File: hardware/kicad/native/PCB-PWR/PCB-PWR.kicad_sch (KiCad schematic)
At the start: 60 parts, among them J1 PWR_INPUT_43045-0213, J2 MAIN_PWR_43045-1202_12PIN, Q1 CSD18540Q5B, U1 LM74700QDBVRQ1, U2 INA226AIDGSR, U3 LMR604403SRAKR 3V8, U4 LMR604403SRAKR 3V3 AON, U5 TPS7A2018PDBVR 1V8_MIC

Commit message: pcb(pwr): bind shared Molex 12-pin footprint
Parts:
- J2: footprint (none) -> DioneyaMain:Molex_43045-1202_MicroFit-12_RA
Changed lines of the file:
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@@
       (effects (font (size 1 1)))
     )
-    (property "Footprint" "" (id 2) (at 198.12 120.22 0)
+    (property "Footprint" "DioneyaMain:Molex_43045-1202_MicroFit-12_RA" (id 2) (at 198.12 120.22 0)
       (effects (font (size 1 1)) hide)
     )

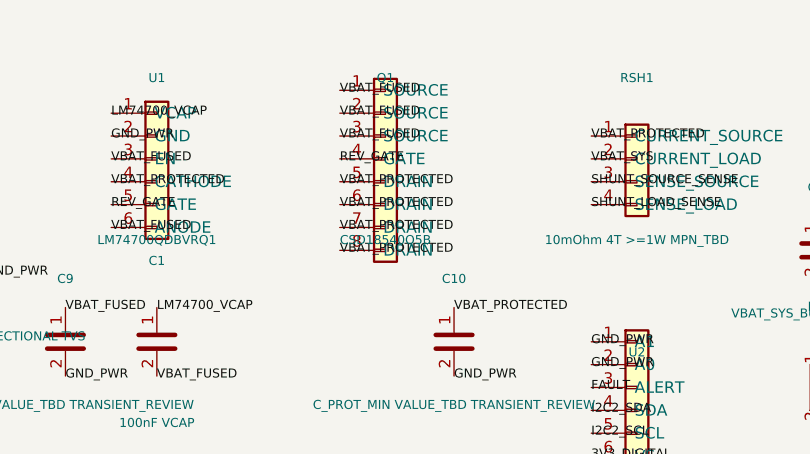
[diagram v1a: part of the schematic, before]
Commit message: fix(pwr): correct CSD18540 physical pin map
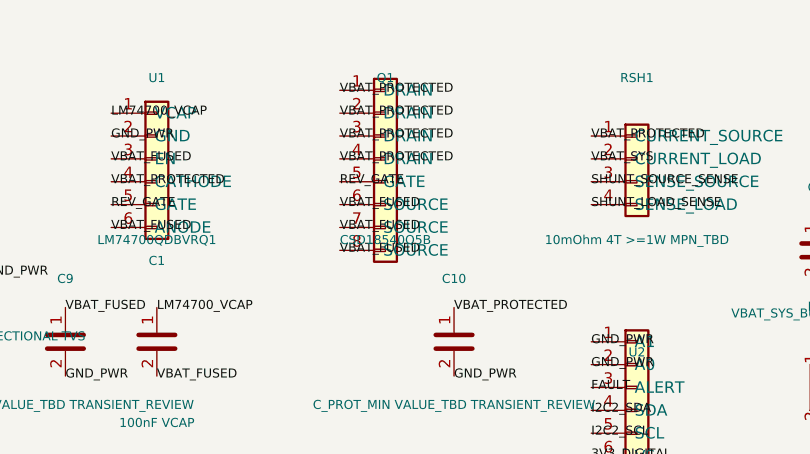
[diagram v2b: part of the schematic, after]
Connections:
- net REV_GATE: now also Q1.5 (GATE); no longer Q1.4 (GATE)
- net VBAT_FUSED: now also Q1.6 (SOURCE), Q1.7 (SOURCE), Q1.8 (SOURCE); no longer Q1.1 (SOURCE), Q1.2 (SOURCE), Q1.3 (SOURCE)
- net VBAT_PROTECTED: now also Q1.1 (DRAIN), Q1.2 (DRAIN), Q1.3 (DRAIN), Q1.4 (DRAIN); no longer Q1.5 (DRAIN), Q1.6 (DRAIN), Q1.7 (DRAIN), Q1.8 (DRAIN)
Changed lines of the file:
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@@
     (effects (font (size 1 1)))
   )
-  (label "VBAT_FUSED" (at 104.14 30.48 0)
+  (label "VBAT_PROTECTED" (at 104.14 30.48 0)
     (effects (font (size 1 1)))
   )
-  (label "VBAT_FUSED" (at 104.14 33.02 0)
+  (label "VBAT_PROTECTED" (at 104.14 33.02 0)
     (effects (font (size 1 1)))
   )
-  (label "VBAT_FUSED" (at 104.14 35.56 0)
+  (label "VBAT_PROTECTED" (at 104.14 35.56 0)
     (effects (font (size 1 1)))
   )
-  (label "REV_GATE" (at 104.14 38.1 0)
+  (label "VBAT_PROTECTED" (at 104.14 38.1 0)
     (effects (font (size 1 1)))
   )
-  (label "VBAT_PROTECTED" (at 104.14 40.64 0)
+  (label "REV_GATE" (at 104.14 40.64 0)
     (effects (font (size 1 1)))
   )
-  (label "VBAT_PROTECTED" (at 104.14 43.18 0)
+  (label "VBAT_FUSED" (at 104.14 43.18 0)
     (effects (font (size 1 1)))
   )
-  (label "VBAT_PROTECTED" (at 104.14 45.72 0)
+  (label "VBAT_FUSED" (at 104.14 45.72 0)
     (effects (font (size 1 1)))
   )
-  (label "VBAT_PROTECTED" (at 104.14 48.26 0)
+  (label "VBAT_FUSED" (at 104.14 48.26 0)
     (effects (font (size 1 1)))
   )

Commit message: Revert "fix(pwr): correct CSD18540 physical pin map"
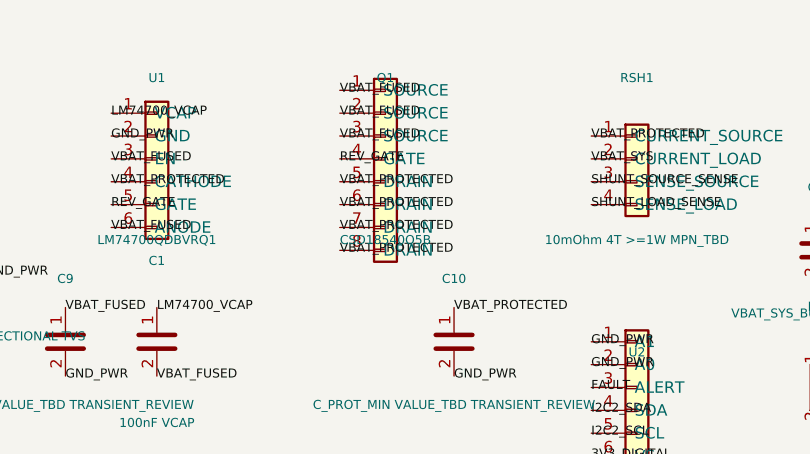
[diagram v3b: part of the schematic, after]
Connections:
- net REV_GATE: now also Q1.4 (GATE); no longer Q1.5 (GATE)
- net VBAT_FUSED: now also Q1.1 (SOURCE), Q1.2 (SOURCE), Q1.3 (SOURCE); no longer Q1.6 (SOURCE), Q1.7 (SOURCE), Q1.8 (SOURCE)
- net VBAT_PROTECTED: now also Q1.5 (DRAIN), Q1.6 (DRAIN), Q1.7 (DRAIN), Q1.8 (DRAIN); no longer Q1.1 (DRAIN), Q1.2 (DRAIN), Q1.3 (DRAIN), Q1.4 (DRAIN)
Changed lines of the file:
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@@
     (effects (font (size 1 1)))
   )
-  (label "VBAT_PROTECTED" (at 104.14 30.48 0)
+  (label "VBAT_FUSED" (at 104.14 30.48 0)
     (effects (font (size 1 1)))
   )
-  (label "VBAT_PROTECTED" (at 104.14 33.02 0)
+  (label "VBAT_FUSED" (at 104.14 33.02 0)
     (effects (font (size 1 1)))
   )
-  (label "VBAT_PROTECTED" (at 104.14 35.56 0)
+  (label "VBAT_FUSED" (at 104.14 35.56 0)
     (effects (font (size 1 1)))
   )
-  (label "VBAT_PROTECTED" (at 104.14 38.1 0)
+  (label "REV_GATE" (at 104.14 38.1 0)
     (effects (font (size 1 1)))
   )
-  (label "REV_GATE" (at 104.14 40.64 0)
+  (label "VBAT_PROTECTED" (at 104.14 40.64 0)
     (effects (font (size 1 1)))
   )
-  (label "VBAT_FUSED" (at 104.14 43.18 0)
+  (label "VBAT_PROTECTED" (at 104.14 43.18 0)
     (effects (font (size 1 1)))
   )
-  (label "VBAT_FUSED" (at 104.14 45.72 0)
+  (label "VBAT_PROTECTED" (at 104.14 45.72 0)
     (effects (font (size 1 1)))
   )
-  (label "VBAT_FUSED" (at 104.14 48.26 0)
+  (label "VBAT_PROTECTED" (at 104.14 48.26 0)
     (effects (font (size 1 1)))
   )

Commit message: pcb(pwr): control CSD18540 footprint
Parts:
- Q1: footprint (none) -> DioneyaPWR:CSD18540Q5B_DNK
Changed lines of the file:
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@@
       (effects (font (size 1 1)))
     )
-    (property "Footprint" "" (id 2) (at 109.22 49.1 0)
+    (property "Footprint" "DioneyaPWR:CSD18540Q5B_DNK" (id 2) (at 109.22 49.1 0)
       (effects (font (size 1 1)) hide)
     )

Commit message: pcb(pwr): control LMR60440 land pattern
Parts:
- U3, U4: footprint (none) -> DioneyaPWR:LMR60440_RAK0009A
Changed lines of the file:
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@@
       (effects (font (size 1 1)))
     )
-    (property "Footprint" "" (id 2) (at 55.88 112.6 0)
+    (property "Footprint" "DioneyaPWR:LMR60440_RAK0009A" (id 2) (at 55.88 112.6 0)
       (effects (font (size 1 1)) hide)
     )
@@
       (effects (font (size 1 1)))
     )
-    (property "Footprint" "" (id 2) (at 121.92 112.6 0)
-      (effects (font (size 1 1)) hide)
-    )
+    (property "Footprint" "DioneyaPWR:LMR60440_RAK0009A" (id 2) (at 121.92 112.6 0)
+      (effects (font (size 1 1)) hide)
+    )

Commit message: pcb(pwr): control TI support IC land patterns
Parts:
- U1: footprint Package_TO_SOT_SMD:SOT-23-6 -> DioneyaPWR:TI_DBV0006A_SOT23-6
- U2: footprint Package_SO:VSSOP-10_3x3mm_P0.5mm -> DioneyaPWR:TI_DGS0010A_VSSOP10
- U5: footprint Package_TO_SOT_SMD:SOT-23-5 -> DioneyaMain:TI_DBV0005A_SOT23-5
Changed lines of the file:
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@@
       (effects (font (size 1 1)))
     )
-    (property "Footprint" "Package_TO_SOT_SMD:SOT-23-6" (id 2) (at 83.82 49.1 0)
+    (property "Footprint" "DioneyaPWR:TI_DBV0006A_SOT23-6" (id 2) (at 83.82 49.1 0)
       (effects (font (size 1 1)) hide)
     )
@@
       (effects (font (size 1 1)))
     )
-    (property "Footprint" "Package_SO:VSSOP-10_3x3mm_P0.5mm" (id 2) (at 137.16 79.58 0)
+    (property "Footprint" "DioneyaPWR:TI_DGS0010A_VSSOP10" (id 2) (at 137.16 79.58 0)
       (effects (font (size 1 1)) hide)
     )
@@
       (effects (font (size 1 1)))
     )
-    (property "Footprint" "Package_TO_SOT_SMD:SOT-23-5" (id 2) (at 68.58 168.48 0)
-      (effects (font (size 1 1)) hide)
-    )
+    (property "Footprint" "DioneyaMain:TI_DBV0005A_SOT23-5" (id 2) (at 68.58 168.48 0)
+      (effects (font (size 1 1)) hide)
+    )

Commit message: pcb(pwr): control remaining component land patterns
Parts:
- J1: footprint (none) -> DioneyaPWR:Molex_43045-0213_MicroFit-2_Vertical
- L1, L2: value 4.7uH >=6A MPN_TBD -> XAL7030-472MEC 4.7uH; footprint (none) -> DioneyaPWR:Coilcraft_XAL7030_472
- RSH1: value 10mOhm 4T >=1W MPN_TBD -> WSK2512R0100FEA 10mOhm 1% 1W 4T; footprint (none) -> DioneyaPWR:Vishay_WSK2512_4T_T1.19mm
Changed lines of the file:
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@@
       (effects (font (size 1 1)))
     )
-    (property "Footprint" "" (id 2) (at 25.4 49.1 0)
-      (effects (font (size 1 1)) hide)
-    )
-    (property "Datasheet" "Molex Micro-Fit 3.0" (id 3) (at 25.4 51.1 0)
+    (property "Footprint" "DioneyaPWR:Molex_43045-0213_MicroFit-2_Vertical" (id 2) (at 25.4 49.1 0)
+      (effects (font (size 1 1)) hide)
+    )
+    (property "Datasheet" "Molex SD-43045-005 Rev.G1" (id 3) (at 25.4 51.1 0)
       (effects (font (size 1 1)) hide)
     )
@@
       (effects (font (size 1 1)))
     )
-    (property "Value" "10mOhm 4T >=1W MPN_TBD" (id 1) (at 137.16 47.1 0)
-      (effects (font (size 1 1)))
-    )
-    (property "Footprint" "" (id 2) (at 137.16 49.1 0)
-      (effects (font (size 1 1)) hide)
-    )
-    (property "Datasheet" "Review-A Kelvin authority" (id 3) (at 137.16 51.1 0)
+    (property "Value" "WSK2512R0100FEA 10mOhm 1% 1W 4T" (id 1) (at 137.16 47.1 0)
+      (effects (font (size 1 1)))
+    )
+    (property "Footprint" "DioneyaPWR:Vishay_WSK2512_4T_T1.19mm" (id 2) (at 137.16 49.1 0)
+      (effects (font (size 1 1)) hide)
+    )
+    (property "Datasheet" "Vishay WSK2512 document 30108" (id 3) (at 137.16 51.1 0)
       (effects (font (size 1 1)) hide)
     )
@@
       (effects (font (size 1 1)))
     )
-    (property "Value" "4.7uH >=6A MPN_TBD" (id 1) (at 81.28 105.52 0)
-      (effects (font (size 1 1)))
-    )
-    (property "Footprint" "" (id 2) (at 81.28 107.52 0)
-      (effects (font (size 1 1)) hide)
-    )
-    (property "Datasheet" "~" (id 3) (at 81.28 109.52 0)
+    (property "Value" "XAL7030-472MEC 4.7uH" (id 1) (at 81.28 105.52 0)
+      (effects (font (size 1 1)))
+    )
+    (property "Footprint" "DioneyaPWR:Coilcraft_XAL7030_472" (id 2) (at 81.28 107.52 0)
+      (effects (font (size 1 1)) hide)
+    )
+    (property "Datasheet" "Coilcraft XAL7030 document 863" (id 3) (at 81.28 109.52 0)
       (effects (font (size 1 1)) hide)
     )
@@
       (effects (font (size 1 1)))
     )
-    (property "Value" "4.7uH >=6A MPN_TBD" (id 1) (at 147.32 105.52 0)
-      (effects (font (size 1 1)))
-    )
-    (property "Footprint" "" (id 2) (at 147.32 107.52 0)
-      (effects (font (size 1 1)) hide)
-    )
-    (property "Datasheet" "~" (id 3) (at 147.32 109.52 0)
-      (effects (font (size 1 1)) hide)
-    )
+    (property "Value" "XAL7030-472MEC 4.7uH" (id 1) (at 147.32 105.52 0)
+      (effects (font (size 1 1)))
+    )
+    (property "Footprint" "DioneyaPWR:Coilcraft_XAL7030_472" (id 2) (at 147.32 107.52 0)
+      (effects (font (size 1 1)) hide)
+    )
+    (property "Datasheet" "Coilcraft XAL7030 document 863" (id 3) (at 147.32 109.52 0)
+      (effects (font (size 1 1)) hide)
+    )

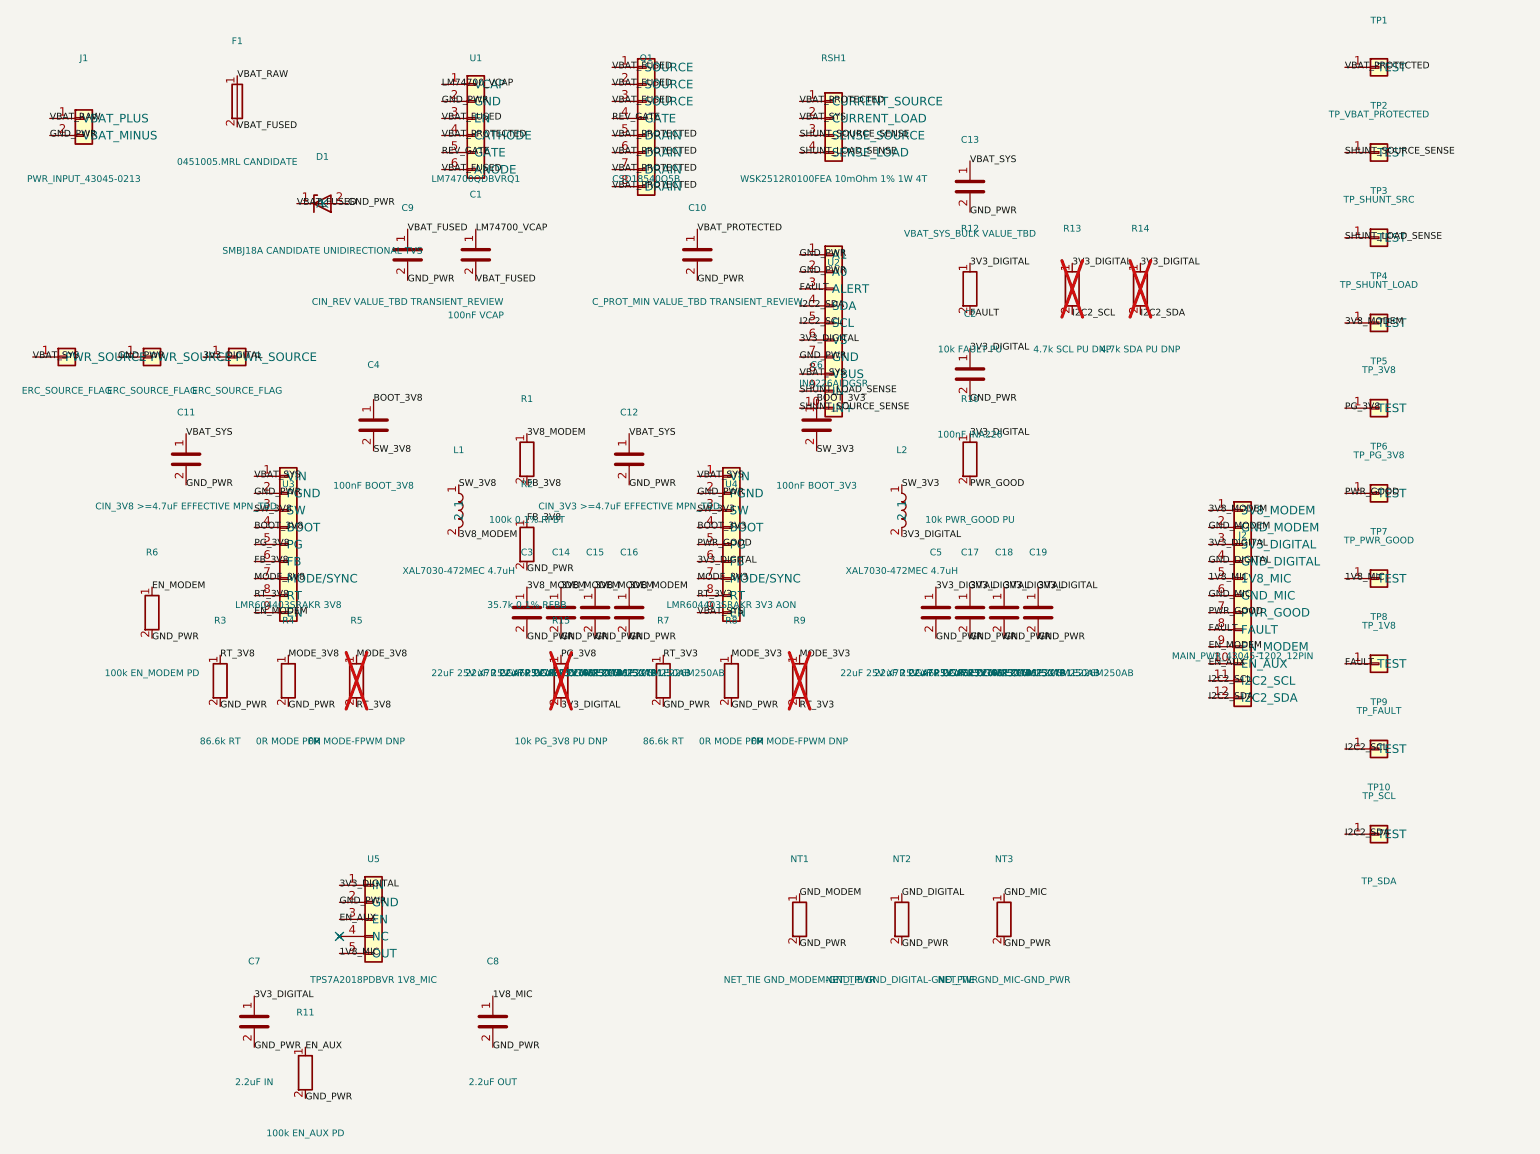
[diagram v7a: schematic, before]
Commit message: pcb(pwr): control passive and DFT authority
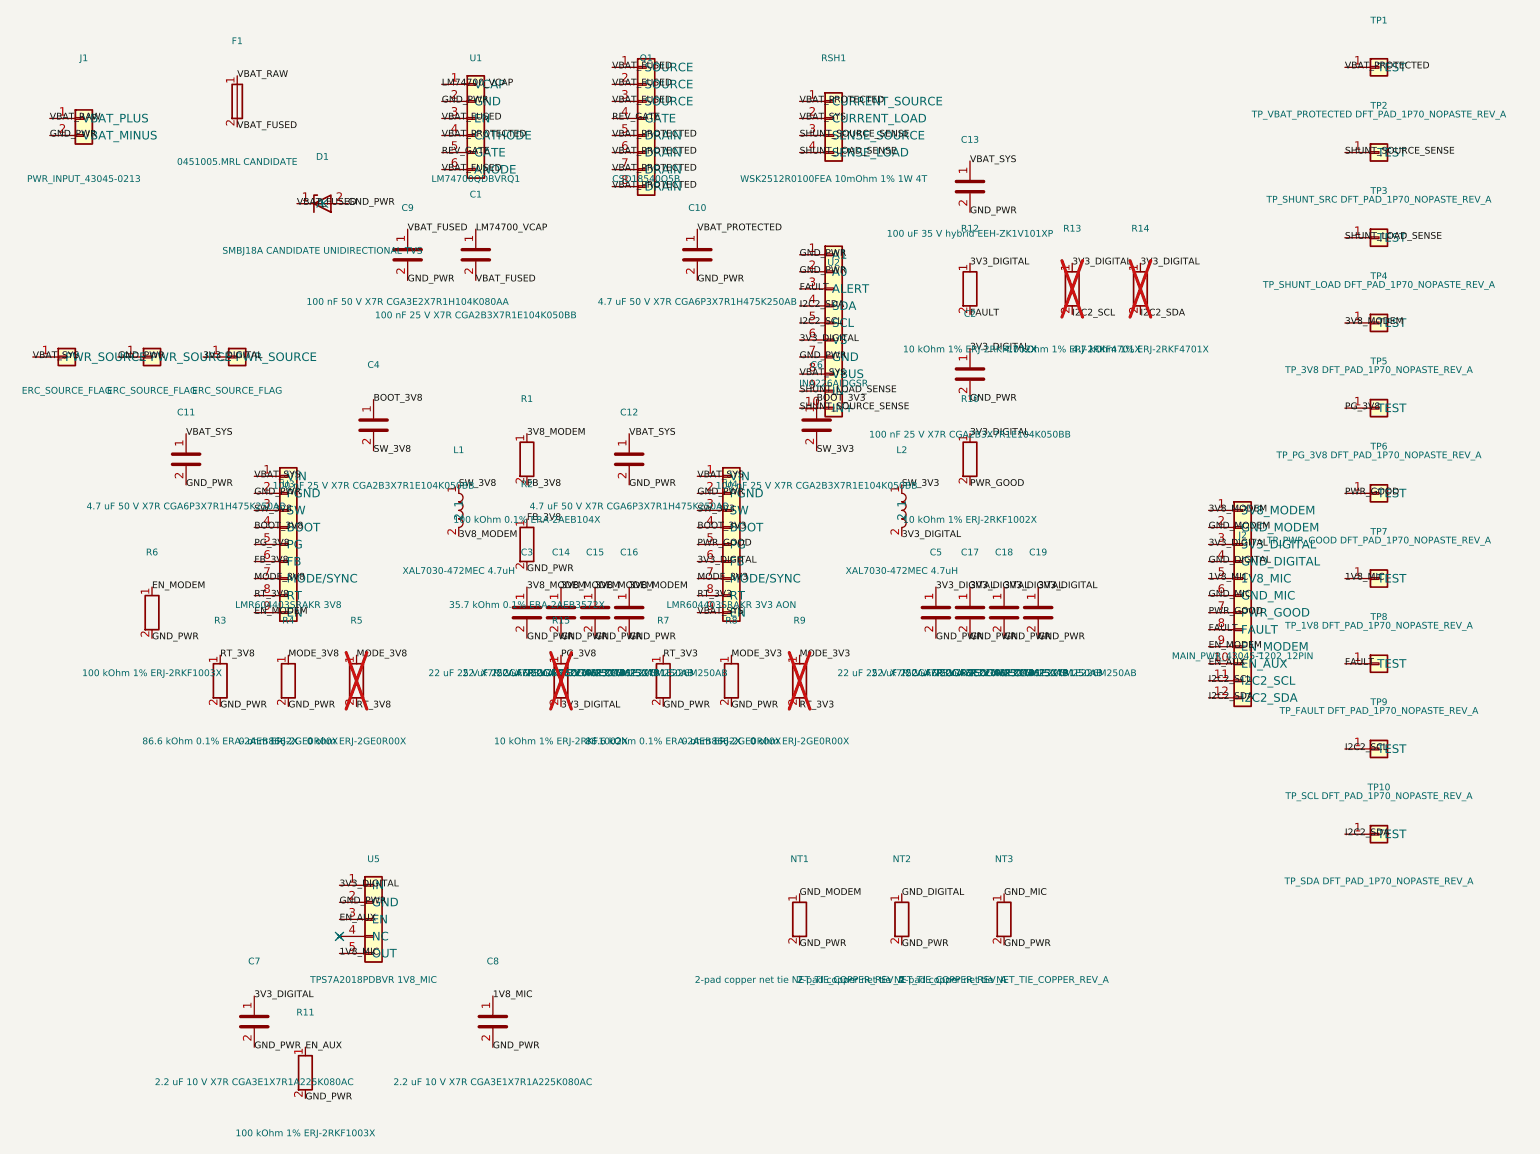
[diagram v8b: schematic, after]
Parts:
- C1: value 100nF VCAP -> 100 nF 25 V X7R CGA2B3X7R1E104K050BB
- C10: value C_PROT_MIN VALUE_TBD TRANSIENT_REVIEW -> 4.7 uF 50 V X7R CGA6P3X7R1H475K250AB; footprint (none) -> Capacitor_SMD:C_1210_3225Metric
- C11: value CIN_3V8 >=4.7uF EFFECTIVE MPN_TBD -> 4.7 uF 50 V X7R CGA6P3X7R1H475K250AB; footprint (none) -> Capacitor_SMD:C_1210_3225Metric
- C12: value CIN_3V3 >=4.7uF EFFECTIVE MPN_TBD -> 4.7 uF 50 V X7R CGA6P3X7R1H475K250AB; footprint (none) -> Capacitor_SMD:C_1210_3225Metric
- C13: value VBAT_SYS_BULK VALUE_TBD -> 100 uF 35 V hybrid EEH-ZK1V101XP; footprint (none) -> Capacitor_SMD:CP_Elec_6.3x7.7
- C14, C15, C16, C17, C18, C19, C3, C5: value 22uF 25V X7R CGA6P3X7R1E226M250AB -> 22 uF 25 V X7R CGA6P3X7R1E226M250AB
- C2: value 100nF INA226 -> 100 nF 25 V X7R CGA2B3X7R1E104K050BB
- C4: value 100nF BOOT_3V8 -> 100 nF 25 V X7R CGA2B3X7R1E104K050BB
- C6: value 100nF BOOT_3V3 -> 100 nF 25 V X7R CGA2B3X7R1E104K050BB
- C7: value 2.2uF IN -> 2.2 uF 10 V X7R CGA3E1X7R1A225K080AC
- C8: value 2.2uF OUT -> 2.2 uF 10 V X7R CGA3E1X7R1A225K080AC
- C9: value CIN_REV VALUE_TBD TRANSIENT_REVIEW -> 100 nF 50 V X7R CGA3E2X7R1H104K080AA; footprint (none) -> Capacitor_SMD:C_0603_1608Metric
- NT1: value NET_TIE GND_MODEM-GND_PWR -> 2-pad copper net tie NET_TIE_COPPER_REV_A
- NT2: value NET_TIE GND_DIGITAL-GND_PWR -> 2-pad copper net tie NET_TIE_COPPER_REV_A
- NT3: value NET_TIE GND_MIC-GND_PWR -> 2-pad copper net tie NET_TIE_COPPER_REV_A
- R1: value 100k 0.1% RFBT -> 100 kOhm 0.1% ERA-2AEB104X
- R10: value 10k PWR_GOOD PU -> 10 kOhm 1% ERJ-2RKF1002X
- R11: value 100k EN_AUX PD -> 100 kOhm 1% ERJ-2RKF1003X
- R12: value 10k FAULT PU -> 10 kOhm 1% ERJ-2RKF1002X
- R13: value 4.7k SCL PU DNP -> 4.7 kOhm 1% ERJ-2RKF4701X
- R14: value 4.7k SDA PU DNP -> 4.7 kOhm 1% ERJ-2RKF4701X
- R15: value 10k PG_3V8 PU DNP -> 10 kOhm 1% ERJ-2RKF1002X
- R2: value 35.7k 0.1% RFBB -> 35.7 kOhm 0.1% ERA-2AEB3572X
- R3, R7: value 86.6k RT -> 86.6 kOhm 0.1% ERA-2AEB8662X
- R4, R8: value 0R MODE PFM -> 0 ohm ERJ-2GE0R00X
- R5, R9: value 0R MODE-FPWM DNP -> 0 ohm ERJ-2GE0R00X
- R6: value 100k EN_MODEM PD -> 100 kOhm 1% ERJ-2RKF1003X
- TP1: value TP_VBAT_PROTECTED -> TP_VBAT_PROTECTED DFT_PAD_1P70_NOPASTE_REV_A; footprint (none) -> DioneyaPWR:TestPoint_DFT_1.7mm_NoPaste
- TP10: value TP_SDA -> TP_SDA DFT_PAD_1P70_NOPASTE_REV_A; footprint (none) -> DioneyaPWR:TestPoint_DFT_1.7mm_NoPaste
- TP2: value TP_SHUNT_SRC -> TP_SHUNT_SRC DFT_PAD_1P70_NOPASTE_REV_A; footprint (none) -> DioneyaPWR:TestPoint_DFT_1.7mm_NoPaste
- TP3: value TP_SHUNT_LOAD -> TP_SHUNT_LOAD DFT_PAD_1P70_NOPASTE_REV_A; footprint (none) -> DioneyaPWR:TestPoint_DFT_1.7mm_NoPaste
- TP4: value TP_3V8 -> TP_3V8 DFT_PAD_1P70_NOPASTE_REV_A; footprint (none) -> DioneyaPWR:TestPoint_DFT_1.7mm_NoPaste
- TP5: value TP_PG_3V8 -> TP_PG_3V8 DFT_PAD_1P70_NOPASTE_REV_A; footprint (none) -> DioneyaPWR:TestPoint_DFT_1.7mm_NoPaste
- TP6: value TP_PWR_GOOD -> TP_PWR_GOOD DFT_PAD_1P70_NOPASTE_REV_A; footprint (none) -> DioneyaPWR:TestPoint_DFT_1.7mm_NoPaste
- TP7: value TP_1V8 -> TP_1V8 DFT_PAD_1P70_NOPASTE_REV_A; footprint (none) -> DioneyaPWR:TestPoint_DFT_1.7mm_NoPaste
- TP8: value TP_FAULT -> TP_FAULT DFT_PAD_1P70_NOPASTE_REV_A; footprint (none) -> DioneyaPWR:TestPoint_DFT_1.7mm_NoPaste
- TP9: value TP_SCL -> TP_SCL DFT_PAD_1P70_NOPASTE_REV_A; footprint (none) -> DioneyaPWR:TestPoint_DFT_1.7mm_NoPaste
